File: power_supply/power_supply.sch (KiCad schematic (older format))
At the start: 0 parts

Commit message: Add components to power supply & update TODO
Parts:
- added C? (x8): CP1, symbol Device:CP1
- added C?: C, symbol Device:C
- added D? (x8): D_ALT, symbol Device:D_ALT
- added D? (x3): LED_ALT, symbol Device:LED_ALT
- added F? (x3): Fuse, symbol Device:Fuse
- added R? (x5): R, symbol Device:R
- added U?: LM7815_TO220, Package_TO_SOT_THT:TO-220-3_Vertical, symbol Regulator_Linear:LM7815_TO220
- added U?: LM7915_TO220, Package_TO_SOT_THT:TO-220-3_Vertical, symbol Regulator_Linear:LM7915_TO220
- added U?: LM7805_TO220, Package_TO_SOT_THT:TO-220-3_Vertical, symbol Regulator_Linear:LM7805_TO220
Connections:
- new net: C?.1, D?.1 (K), U?.1 (VI)
- new net: C?.2, D?.1 (K), U?.2 (VI)
- new net GNDPWR: C?.1, C?.1, C?.1, C?.2, C?.2, C?.2, D?.1 (K), D?.2 (A), U?.1 (GND), U?.2 (GND)
- new net VCC: C?.1, C?.1, D?.1 (K), D?.2 (A), U?.3 (VO)
- new net VEE: C?.2, C?.2, D?.2 (A), D?.2 (A), U?.3 (VO)
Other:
- note added: "Maybe use 9V or 15V?"
- note added: "TODO\nsecondary fuses necessary?\nfuse/line filter/power entry module\nswitch\nmaybe use 9V/15V for relays?\nsplit power supply startup problems?"

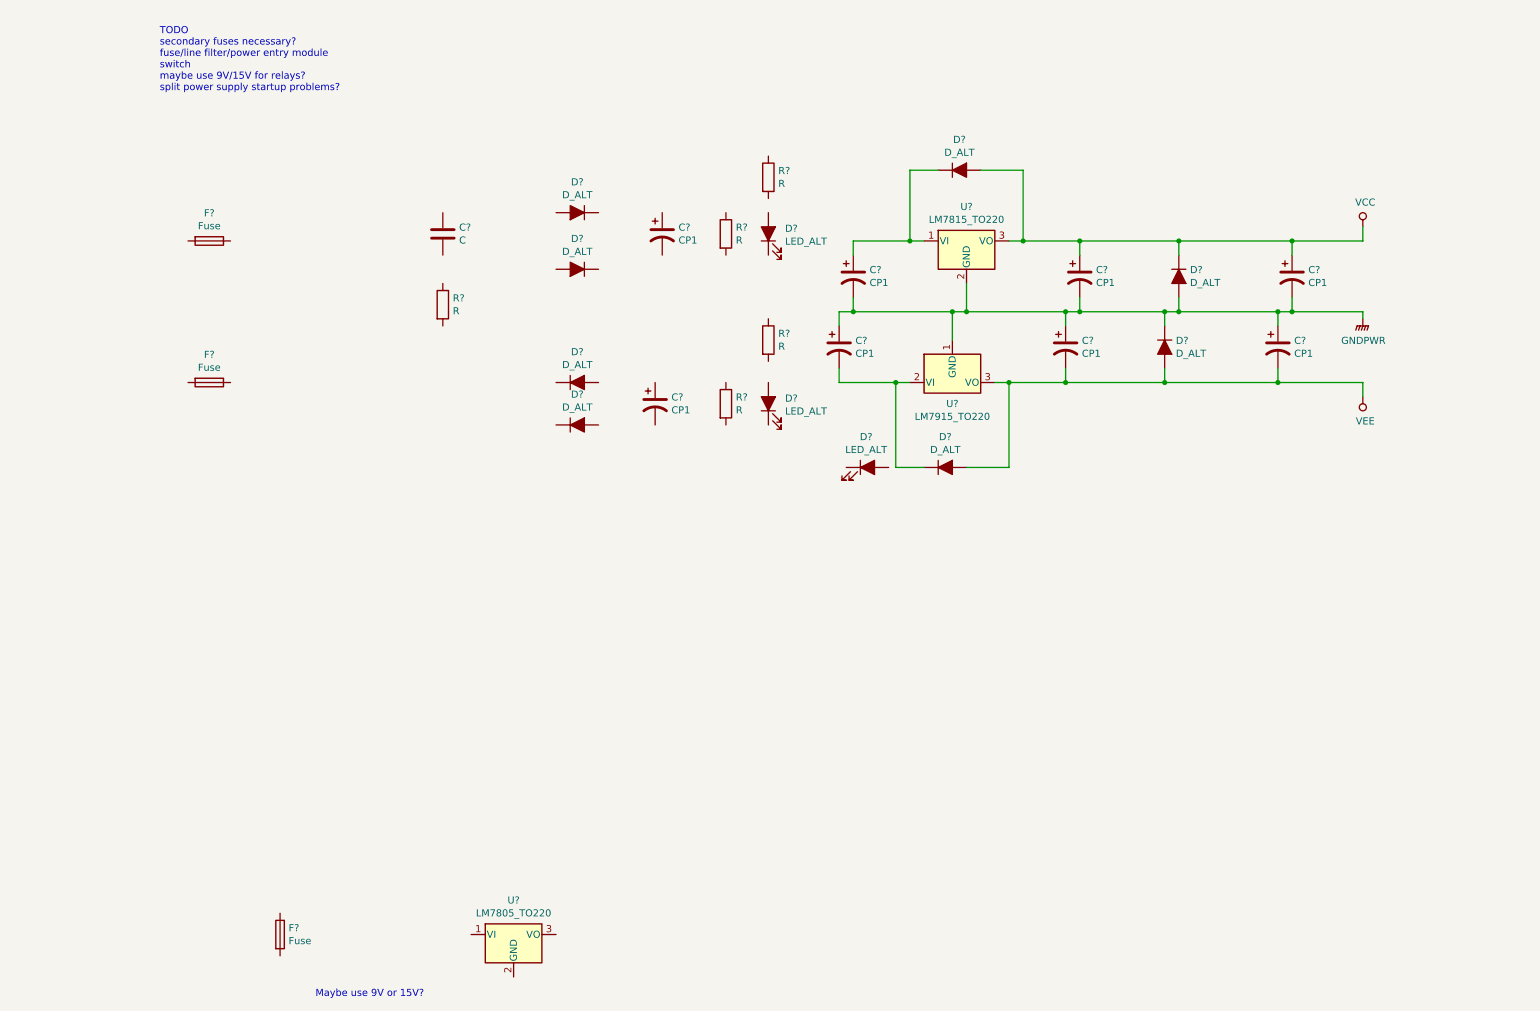
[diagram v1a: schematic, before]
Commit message: Draw connections for primary split power supply
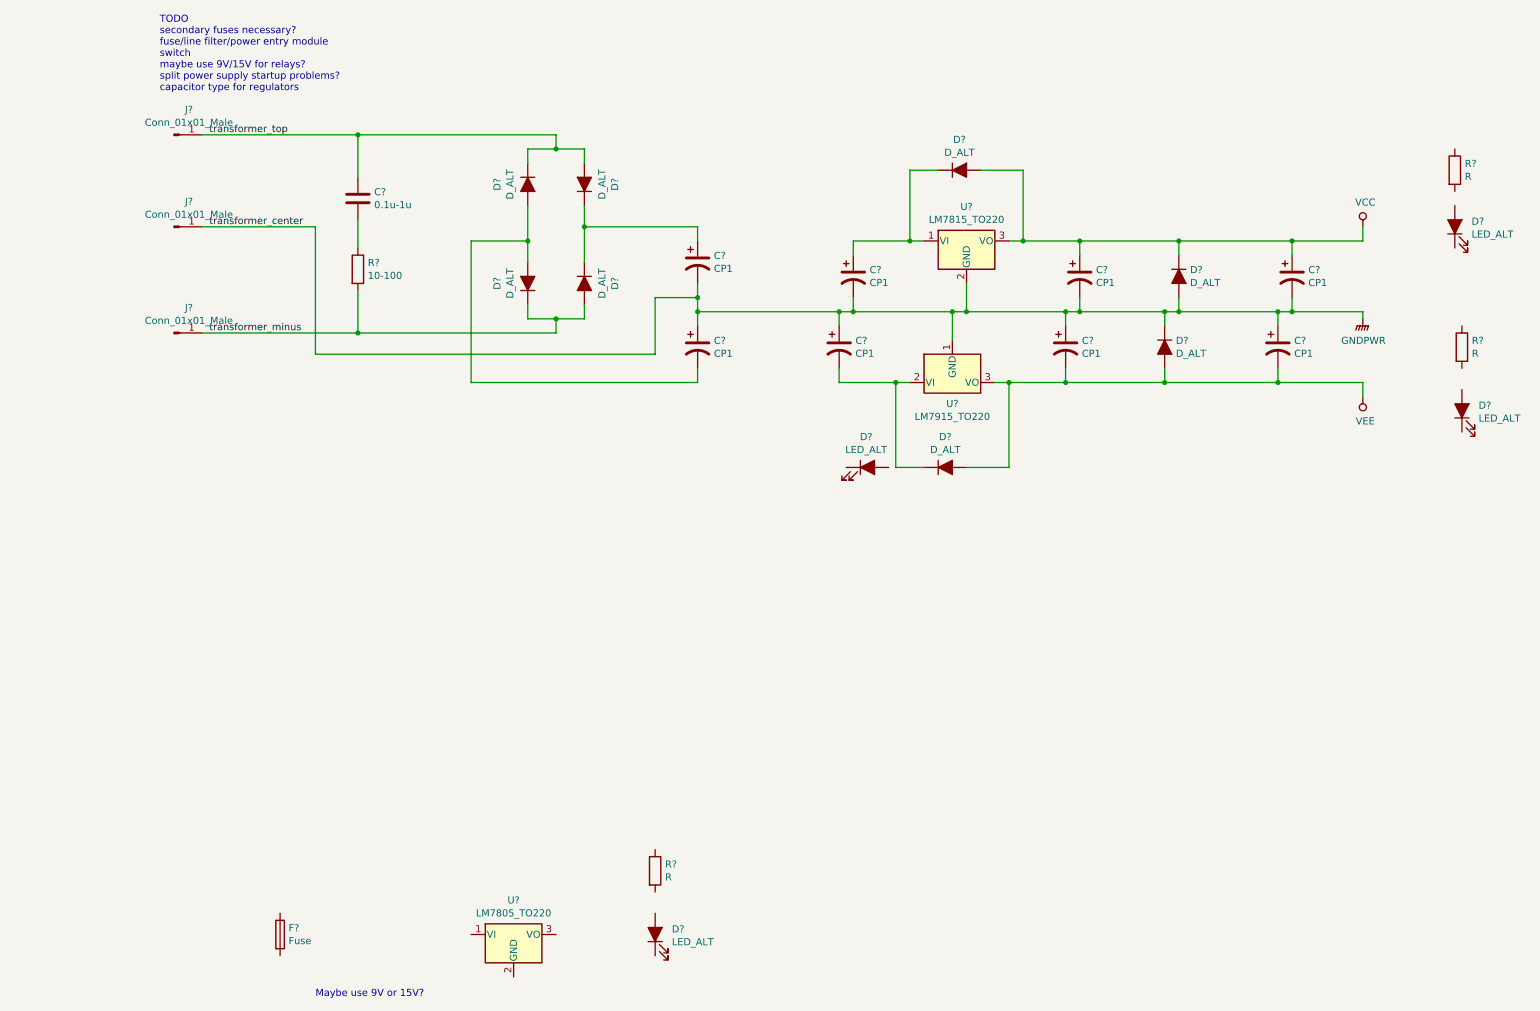
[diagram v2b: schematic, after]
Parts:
- removed F? (x2): Fuse, symbol Device:Fuse
- removed R? (x2): R, symbol Device:R
- added D?: LED_ALT, symbol Device:LED_ALT
- added J? (x3): Conn_01x01_Male, symbol Connector:Conn_01x01_Male
- added R?: R, symbol Device:R
- C?: value C -> 0.1u-1u
- R?: value R -> 10-100
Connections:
- net GNDPWR: now also C?.1, C?.2, J?.1 (Pin_1)
- net transformer_top: now reaches D?.1 (K)
- net transformer_top: now also C?.1, D?.2 (A), J?.1 (Pin_1)
- net at D?.2 (A): now also C?.2, D?.2 (A)
- net at D?.1 (K): now also C?.1, D?.1 (K)
- net transformer_minus: now reaches D?.2 (A)
- net transformer_minus: now also D?.1 (K), R?.2, J?.1 (Pin_1)
- net at C?.2: now also R?.1
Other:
- note added: "TODO\nsecondary fuses necessary?\nfuse/line filter/power entry module\nswitch\nmaybe use 9V/15V for relays?\nsplit power supply startup problems?\ncapacitor type for regulators"
- note removed: "TODO\nsecondary fuses necessary?\nfuse/line filter/power entry module\nswitch\nmaybe use 9V/15V for relays?\nsplit power supply startup problems?"
- moved on the sheet: C?, D?, R?

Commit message: Update some values and connections
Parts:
- C? (x2): value CP1 -> 100u
- C? (x2): value CP1 -> 4700u?
- D? (x4): value D_ALT -> 1N4007
- R? (x2): value R -> 1k
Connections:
- net VEE: now also D?.1 (K); no longer D?.2 (A)
- net at C?.1, D?.1 (K), U?.1 (VI): now also C?.1, D?.1 (K), D?.1 (K)
- net at C?.2, U?.2 (VI): now also C?.2, D?.2 (A), D?.2 (A), D?.2 (A); no longer D?.1 (K)
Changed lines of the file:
@@
 P 6350 3600
 F 0 "D?" H 6350 3816 50  0000 C CNN
-F 1 "D_ALT" H 6350 3725 50  0000 C CNN
+F 1 "1N4007" H 6350 3725 50  0000 C CNN
 F 2 "" H 6350 3600 50  0001 C CNN
 F 3 "~" H 6350 3600 50  0001 C CNN
 	1    6350 3600
-	1    0    0    -1
+	-1   0    0    1
 $EndComp
 $Comp
@@
 P 6450 1500
 F 0 "D?" H 6450 1716 50  0000 C CNN
-F 1 "D_ALT" H 6450 1625 50  0000 C CNN
+F 1 "1N4007" H 6450 1625 50  0000 C CNN
 F 2 "" H 6450 1500 50  0001 C CNN
 F 3 "~" H 6450 1500 50  0001 C CNN
@@
 P 7300 2250
 F 0 "C?" H 7415 2296 50  0000 L CNN
-F 1 "CP1" H 7415 2205 50  0000 L CNN
+F 1 "100u" H 7415 2205 50  0000 L CNN
 F 2 "" H 7300 2250 50  0001 C CNN
 F 3 "~" H 7300 2250 50  0001 C CNN
@@
 P 7200 2750
 F 0 "C?" H 7315 2796 50  0000 L CNN
-F 1 "CP1" H 7315 2705 50  0000 L CNN
+F 1 "100u" H 7315 2705 50  0000 L CNN
 F 2 "" H 7200 2750 50  0001 C CNN
 F 3 "~" H 7200 2750 50  0001 C CNN
@@
 P 8000 2250
 F 0 "D?" V 7954 2329 50  0000 L CNN
-F 1 "D_ALT" V 8045 2329 50  0000 L CNN
+F 1 "1N4007" V 8045 2329 50  0000 L CNN
 F 2 "" H 8000 2250 50  0001 C CNN
 F 3 "~" H 8000 2250 50  0001 C CNN
@@
 P 7900 2750
 F 0 "D?" V 7854 2829 50  0000 L CNN
-F 1 "D_ALT" V 7945 2829 50  0000 L CNN
+F 1 "1N4007" V 7945 2829 50  0000 L CNN
 F 2 "" H 7900 2750 50  0001 C CNN
 F 3 "~" H 7900 2750 50  0001 C CNN
@@
 P 4600 2150
 F 0 "C?" H 4715 2196 50  0000 L CNN
-F 1 "CP1" H 4715 2105 50  0000 L CNN
+F 1 "4700u?" H 4715 2105 50  0000 L CNN
 F 2 "" H 4600 2150 50  0001 C CNN
 F 3 "~" H 4600 2150 50  0001 C CNN
@@
 P 4600 2750
 F 0 "C?" H 4715 2796 50  0000 L CNN
-F 1 "CP1" H 4715 2705 50  0000 L CNN
+F 1 "4700u?" H 4715 2705 50  0000 L CNN
 F 2 "" H 4600 2750 50  0001 C CNN
 F 3 "~" H 4600 2750 50  0001 C CNN
@@
 P 9950 1500
 F 0 "R?" H 10020 1546 50  0000 L CNN
-F 1 "R" H 10020 1455 50  0000 L CNN
+F 1 "1k" H 10020 1455 50  0000 L CNN
 F 2 "" V 9880 1500 50  0001 C CNN
 F 3 "~" H 9950 1500 50  0001 C CNN
@@
 P 10000 2750
 F 0 "R?" H 10070 2796 50  0000 L CNN
-F 1 "R" H 10070 2705 50  0000 L CNN
+F 1 "1k" H 10070 2705 50  0000 L CNN
 F 2 "" V 9930 2750 50  0001 C CNN
 F 3 "~" H 10000 2750 50  0001 C CNN
@@
 Text Label 1150 1250 0    50   ~ 0
 transformer_top
+Wire Wire Line
+	4600 3000 5600 3000
+Connection ~ 4600 3000
+Connection ~ 5600 3000
+Wire Wire Line
+	4600 1900 5700 1900
+Wire Wire Line
+	5700 1900 5700 2000
+Connection ~ 4600 1900
+Connection ~ 5700 2000
 $EndSCHEMATC

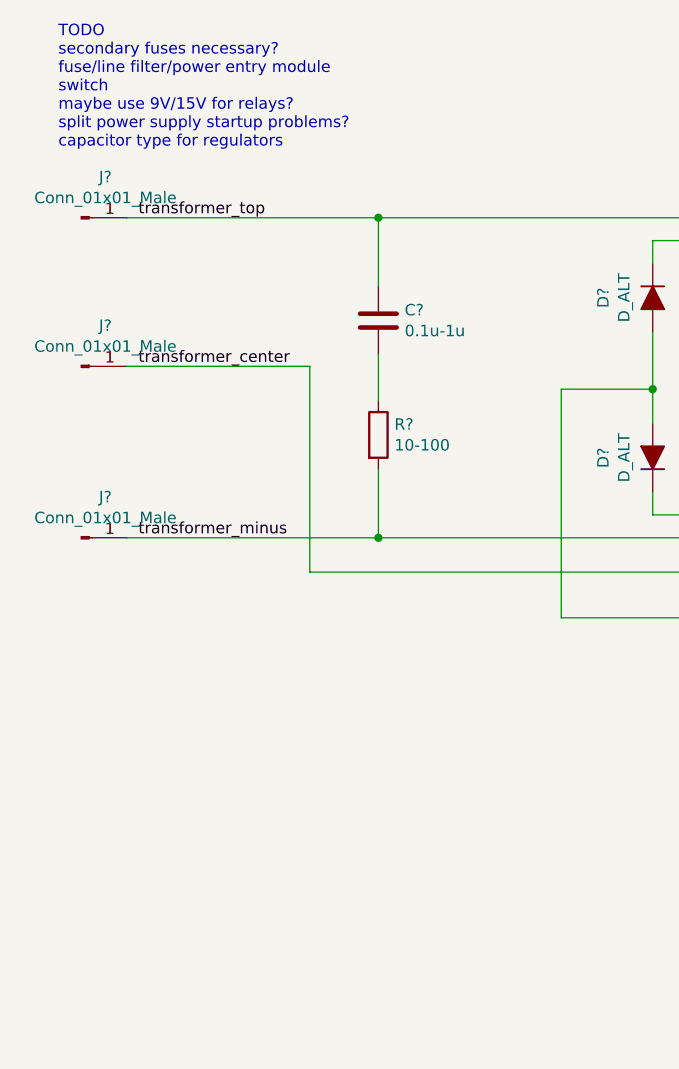
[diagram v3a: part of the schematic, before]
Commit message: Update TODO (current measurement headers)
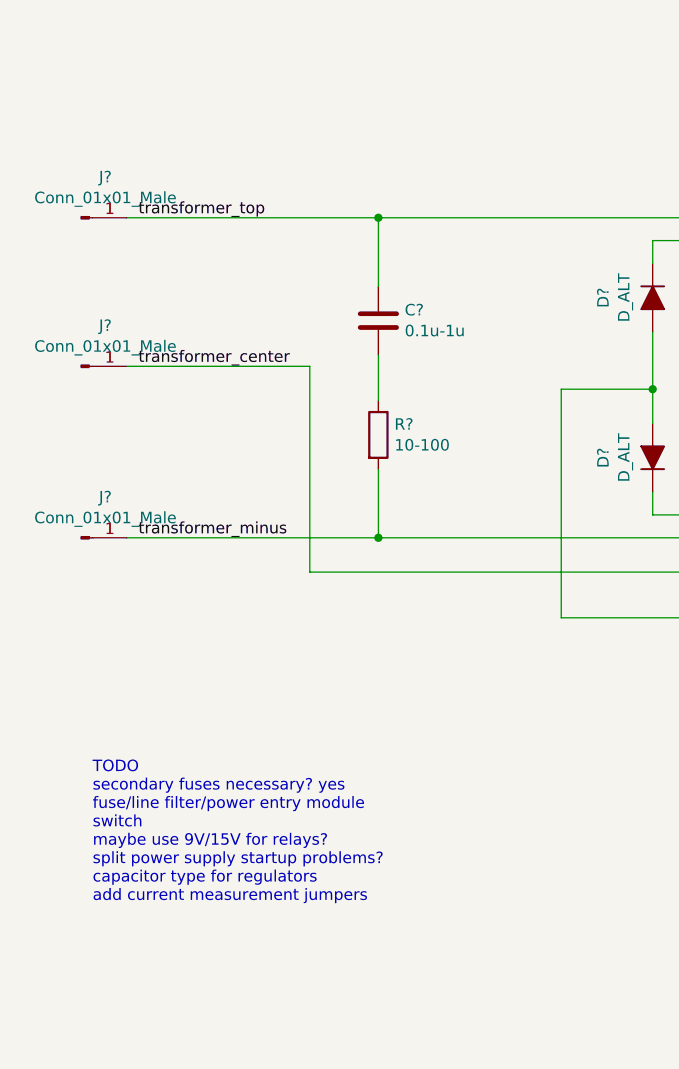
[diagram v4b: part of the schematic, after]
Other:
- note added: "TODO\nsecondary fuses necessary? yes\nfuse/line filter/power entry module\nswitch\nmaybe use 9V/15V for relays?\nsplit power supply startup problems?\ncapacitor type for regulators\nadd current measurement jumpers"
- note removed: "TODO\nsecondary fuses necessary?\nfuse/line filter/power entry module\nswitch\nmaybe use 9V/15V for relays?\nsplit power supply startup problems?\ncapacitor type for regulators"
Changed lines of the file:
@@
 EESchema Schematic File Version 4
 LIBS:power_supply-cache
-EELAYER 26 0
+EELAYER 29 0
 EELAYER END
 $Descr A 11000 8500
@@
 Text Notes 1900 7350 0    50   ~ 0
 Maybe use 9V or 15V?
-Text Notes 800  950  0    50   ~ 0
-TODO\nsecondary fuses necessary?\nfuse/line filter/power entry module\nswitch\nmaybe use 9V/15V for relays?\nsplit power supply startup problems?\ncapacitor type for regulators
+Text Notes 950  4250 0    50   ~ 0
+TODO\nsecondary fuses necessary? yes\nfuse/line filter/power entry module\nswitch\nmaybe use 9V/15V for relays?\nsplit power supply startup problems?\ncapacitor type for regulators\nadd current measurement jumpers
 $Comp
 L Device:R R?

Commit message: Update power supply schematic
add jumpers for measuring current
remove redundant capacitors
wire LEDs
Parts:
- removed C? (x3): CP1, symbol Device:CP1
- removed D?: LED_ALT, symbol Device:LED_ALT
- added C?: 330n, symbol Device:C
- added JP1, JP2, JP3, JP4, JP5: Jumper_NC_Small, symbol Device:Jumper_NC_Small
- C?: value CP1 -> 330n; symbol Device:CP1 -> Device:C
- C? (x2): value 4700u? -> 1000u
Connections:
- net GNDPWR: now also D?.1 (K), R?.2, C?.1, JP4.2; no longer J?.1 (Pin_1)
- net VCC: now also R?.1
- net VEE: now also D?.1 (K)
- net transformer_minus: now also JP2.1; no longer D?.1 (K), D?.2 (A), R?.2
- net transformer_top: now also JP1.1; no longer C?.1, D?.1 (K), D?.2 (A)
- net at C?.1, C?.1, D?.1 (K)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: now also JP3.2; no longer D?.1 (K), D?.1 (K)
- net at C?.2, D?.2 (A), U?.2 (VI): now also C?.2, JP5.2; no longer D?.2 (A), D?.2 (A)
- net at D?.2 (A): now also R?.2
- net at D?.2 (A): now also R?.1
- new net: C?.1, D?.1 (K), D?.2 (A), JP1.2
- new net: D?.2 (A), D?.2 (A), JP5.1
- new net: D?.1 (K), D?.1 (K), JP3.1
- new net: D?.1 (K), D?.2 (A), JP2.2, R?.2
- new net transformer_center: J?.1 (Pin_1), JP4.1
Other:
- note added: "RESERVOIR CAPACITORS\n\nVpp = I * dt / C\n\nI = 100mA (measured 76mA)\ndt = 6ms (SSAD p710, adjusted for 60Hz mains)\nC = ?\n\nVpp = 1V -> C = 600uF\nVpp = 2V -> 300uF"
- note added: "TODO\nsecondary fuses necessary? yes\nmaybe use 9V/15V for relays?\nsplit power supply startup problems?\ncapacitor type for regulators\nsee if 10k resistors will work for LEDs"
- note removed: "TODO\nsecondary fuses necessary? yes\nfuse/line filter/power entry module\nswitch\nmaybe use 9V/15V for relays?\nsplit power supply startup problems?\ncapacitor type for regulators\nadd current measurement jumpers"
- moved on the sheet: C?, D?, R?
